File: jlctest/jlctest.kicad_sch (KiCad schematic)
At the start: 44 parts, among them Q1 MMBT5551_C2145, Q2 S8550_C105432, Q3 SI2301CDS-T1-GE3, Q4 AO3401A, Q5 D882_C9634, SW1 TS-1187A-B-A-B, U1 OP07CDR, U10 L78M05ABDT-TR, U2 TPS5430DDAR, U3 SP485EEN-L/TR, U4 W25Q128JVSIQTR, U5 LM324DT, U6 74HC595D,118, U7 SP3232EEY-L/TR, U8 AMS1117-3.3, U9 AMS1117-5.0, X1 X322516MLB4SI, X2 Q13FC1350000400, X3 X322512MSB4SI, X4 X49SM8MSD2SC, X5 X50328MSB2GI

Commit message: fixup script developed and run
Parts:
- C1: PartNumber (none) -> 0402B102K500NT
- C2: PartNumber (none) -> 0603B103K500NT
- C3: PartNumber (none) -> 0805B333K500NT
- C4: PartNumber (none) -> 1206B102K202NT
- C5: PartNumber (none) -> TAJA106K016RNJ
- C6: PartNumber (none) -> TAJB107K006RNJ
- D1: PartNumber (none) -> SS34_C8678
- D2: PartNumber (none) -> SS54_C22452
- D3: PartNumber (none) -> US1MG_C412437
- D4: PartNumber (none) -> P6SMB6.8CA-C78395
- D5: PartNumber (none) -> 1N4148W_C81598
- D6: PartNumber (none) -> SM4007PL
- D7: PartNumber (none) -> B5819W_C8598
- D8: PartNumber (none) -> 1N4148WS T4
- L1: PartNumber (none) -> GZ1608D601TF
- L2: PartNumber (none) -> GZ2012D101TF
- LED1: PartNumber (none) -> whiteLEDSMD
- Q1: PartNumber (none) -> MMBT5551_C2145
- Q2: PartNumber (none) -> S8550_C105432
- Q3: PartNumber (none) -> SI2301CDS-T1-GE3
- Q4: PartNumber (none) -> AO3401A
- Q5: PartNumber (none) -> D882_C9634
- R1: PartNumber (none) -> 0402WGF0000TCE
- R2: PartNumber (none) -> 0603WAF0000T5E
- R3: PartNumber (none) -> 0805W8F0000T5E
- R4: PartNumber (none) -> 1206W4F0000T5E
- R5: PartNumber (none) -> 0805W8F100JT5E
- RN1: PartNumber (none) -> 4D03WGJ0102T5E
- SW1: PartNumber (none) -> TS-1187A-B-A-B
- U1: PartNumber (none) -> OP07CDR
- U10: PartNumber (none) -> L78M05ABDT-TR
- U2: PartNumber (none) -> TPS5430DDAR
- U3: PartNumber (none) -> SP485EEN-L/TR
- U4: PartNumber (none) -> W25Q128JVSIQTR
- U5: PartNumber (none) -> LM324DT
- U6: PartNumber (none) -> 74HC595D,118
- U7: PartNumber (none) -> SP3232EEY-L/TR
- U8: PartNumber (none) -> AMS1117-3.3
- U9: PartNumber (none) -> AMS1117-5.0
- X1: PartNumber (none) -> X322516MLB4SI
- X2: PartNumber (none) -> Q13FC1350000400
- X3: PartNumber (none) -> X322512MSB4SI
- X4: PartNumber (none) -> X49SM8MSD2SC
- X5: PartNumber (none) -> X50328MSB2GI

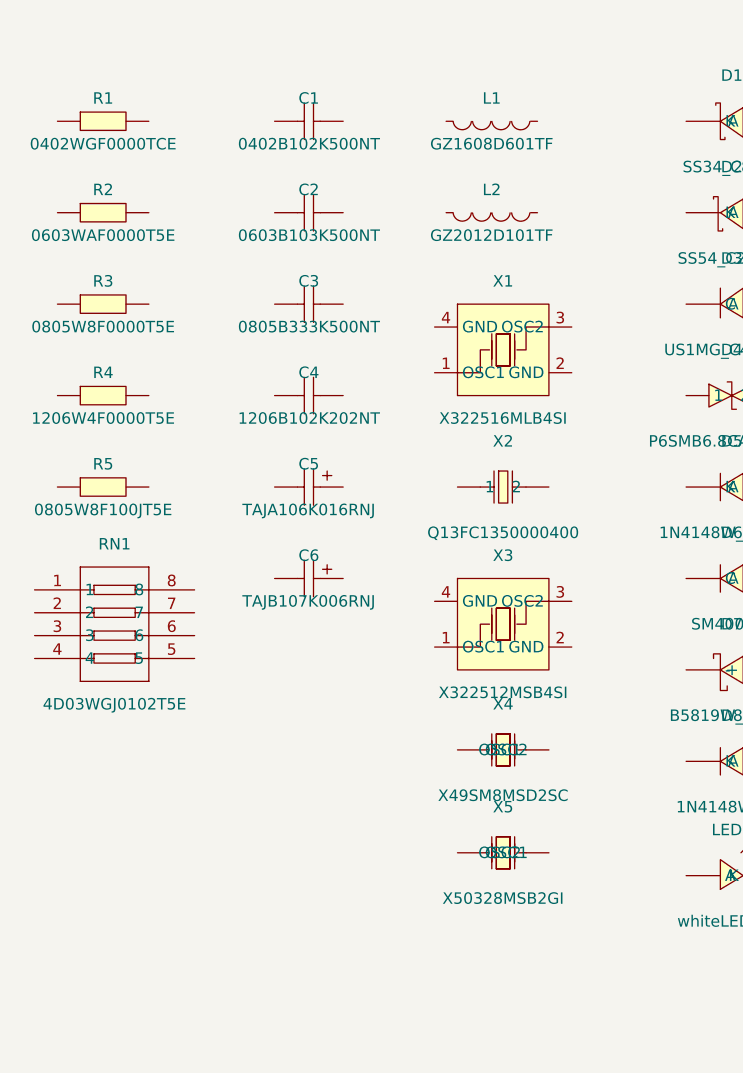
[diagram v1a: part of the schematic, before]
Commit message: Updated symbols with values and descriptions from screen scrapings
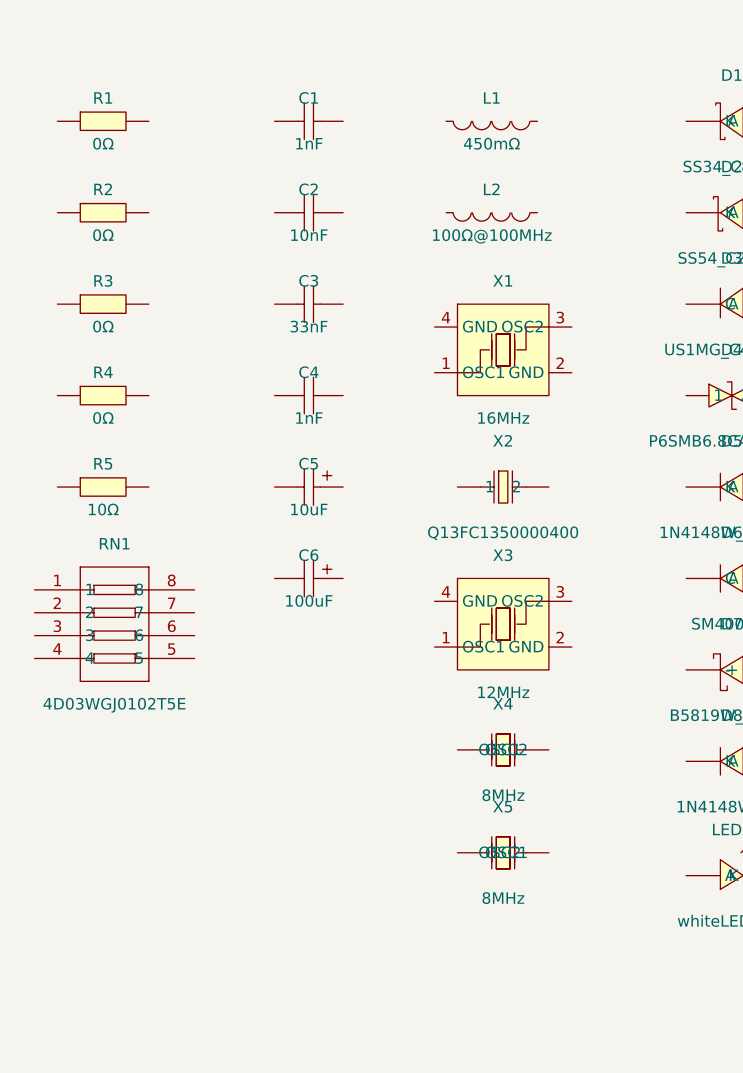
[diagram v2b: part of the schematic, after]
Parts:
- C1: value 0402B102K500NT -> 1nF
- C2: value 0603B103K500NT -> 10nF
- C3: value 0805B333K500NT -> 33nF
- C4: value 1206B102K202NT -> 1nF
- C5: value TAJA106K016RNJ -> 10uF
- C6: value TAJB107K006RNJ -> 100uF
- L1: value GZ1608D601TF -> 450mΩ
- L2: value GZ2012D101TF -> 100Ω@100MHz
- R1: value 0402WGF0000TCE -> 0Ω
- R2: value 0603WAF0000T5E -> 0Ω
- R3: value 0805W8F0000T5E -> 0Ω
- R4: value 1206W4F0000T5E -> 0Ω
- R5: value 0805W8F100JT5E -> 10Ω
- X1: value X322516MLB4SI -> 16MHz
- X3: value X322512MSB4SI -> 12MHz
- X4: value X49SM8MSD2SC -> 8MHz
- X5: value X50328MSB2GI -> 8MHz
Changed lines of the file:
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@@
 			)
 		)
-		(property "Description" ""
+		(property "Description" "235Kbps Transceiver 2/2 TSSOP-16 RS232 ICs ROHS"
 			(at 201.93 121.92 0)
 			(effects
@@
 			)
 		)
-		(property "Description" ""
+		(property "Description" "20V 3.1A 112mΩ@4.5V,2.8A 1V@250uA 1 Piece P-Channel SOT-23 MOSFETs ROHS"
 			(at 130.81 83.82 0)
 			(effects
@@
 			)
 		)
-		(property "Description" ""
+		(property "Description" "30V 4A 44mΩ@10V,4.3A 1.4W 1.3V@250uA 1 Piece P-Channel SOT-23 MOSFETs ROHS"
 			(at 129.54 97.79 0)
 			(effects
@@
 			)
 		)
-		(property "Value" "0805B333K500NT"
+		(property "Value" "33nF"
 			(at 66.04 76.2 0)
 			(effects
@@
 			)
 		)
-		(property "Description" ""
+		(property "Description" "50V 33nF X7R ±10% 0805 Multilayer Ceramic Capacitors MLCC - SMD/SMT ROHS"
 			(at 66.04 73.66 0)
 			(effects
@@
 			)
 		)
-		(property "Value" "TAJA106K016RNJ"
+		(property "Value" "10uF"
 			(at 66.04 96.52 0)
 			(effects
@@
 			)
 		)
-		(property "Description" ""
+		(property "Description" "10uF 16V 3Ω@100kHz ±10% CASE-A-3216-18(mm) Tantalum Capacitors ROHS"
 			(at 66.04 93.98 0)
 			(effects
@@
 			)
 		)
-		(property "Value" "1206B102K202NT"
+		(property "Value" "1nF"
 			(at 66.04 86.36 0)
 			(effects
@@
 			)
 		)
-		(property "Description" ""
+		(property "Description" "2kV 1nF X7R ±10% 1206 Multilayer Ceramic Capacitors MLCC - SMD/SMT ROHS"
 			(at 66.04 83.82 0)
 			(effects
@@
 			)
 		)
-		(property "Description" ""
+		(property "Description" "8 2V~6V 1 Serial to serial or parallel SOIC-16 Shift Registers ROHS"
 			(at 201.93 91.44 0)
 			(effects
@@
 			)
 		)
-		(property "Value" "0402WGF0000TCE"
+		(property "Value" "0Ω"
 			(at 43.18 55.88 0)
 			(effects
@@
 			)
 		)
-		(property "Description" ""
+		(property "Description" "62.5mW Thick Film Resistors 50V ±800ppm/℃ ±1% 0Ω 0402 Chip Resistor - Surface Mount ROHS"
 			(at 43.18 53.34 0)
 			(effects
@@
 			)
 		)
-		(property "Description" ""
+		(property "Description" "1A Independent Type 1kV 1.1V@1A SOD-123FL Diodes - General Purpose ROHS"
 			(at 113.03 104.14 0)
 			(effects
@@
 			)
 		)
-		(property "Description" ""
+		(property "Description" "Quad 20nA 0.4V/us 1.3MHz SOIC-14 Operational Amplifier ROHS"
 			(at 201.93 60.96 0)
 			(effects
@@
 			)
 		)
-		(property "Value" "TAJB107K006RNJ"
+		(property "Value" "100uF"
 			(at 66.04 106.68 0)
 			(effects
@@
 			)
 		)
-		(property "Description" ""
+		(property "Description" "100uF 6.3V 1.7Ω@100kHz ±10% CASE-B-3528-21(mm) Tantalum Capacitors ROHS"
 			(at 66.04 104.14 0)
 			(effects
@@
 			)
 		)
-		(property "Description" ""
+		(property "Description" "Transceiver 10Mbps 1/1 SOIC-8 RS-485 / RS-422 ICs ROHS"
 			(at 166.37 115.57 0)
 			(effects
@@
 			)
 		)
-		(property "Value" "GZ1608D601TF"
+		(property "Value" "450mΩ"
 			(at 86.36 55.88 0)
 			(effects
@@
 			)
 		)
-		(property "Description" ""
+		(property "Description" "450mΩ ±25% 600Ω@100MHz 0603 Ferrite Beads ROHS"
 			(at 86.36 53.34 0)
 			(effects
@@
 			)
 		)
-		(property "Description" ""
+		(property "Description" "None Without 50mA 5.1mm 100000 Times 160gf 12V 5.1mm 1.5mm Round Button Standing paste SPST SMD Tactile Switches ROHS"
 			(at 234.95 120.65 0)
 			(effects
@@
 			)
 		)
-		(property "Description" ""
+		(property "Description" "600kHz 1.8nA Single Channel SOIC-8 Precision Op Amps ROHS"
 			(at 163.83 60.96 0)
 			(effects
@@
 			)
 		)
-		(property "Value" "X49SM8MSD2SC"
+		(property "Value" "8MHz"
 			(at 87.63 128.27 0)
 			(effects
@@
 			)
 		)
-		(property "Description" ""
+		(property "Description" "8MHz Surface Mount Crystal 20pF ±20ppm ±30ppm HC-49S-SMD Crystals ROHS"
 			(at 87.63 123.19 0)
 			(effects
@@
 			)
 		)
-		(property "Description" ""
+		(property "Description" "Step-down type Adjustable 1.221V~32.04V 3A 5.5V~36V SOIC-8-EP DC-DC Converters ROHS"
 			(at 165.1 90.17 0)
 			(effects
@@
 			)
 		)
-		(property "Value" "X50328MSB2GI"
+		(property "Value" "8MHz"
 			(at 87.63 139.7 0)
 			(effects
@@
 			)
 		)
-		(property "Description" ""
+		(property "Description" "8MHz Surface Mount Crystal 20pF ±10ppm ±20ppm SMD5032 Crystals ROHS"
 			(at 87.63 134.62 0)
 			(effects
@@
 			)
 		)
-		(property "Value" "1206W4F0000T5E"
+		(property "Value" "0Ω"
 			(at 43.18 86.36 0)
 			(effects
@@
 			)
 		)
-		(property "Description" ""
+		(property "Description" "250mW Thick Film Resistors 200V ±800ppm/℃ ±1% 0Ω 1206 Chip Resistor - Surface Mount ROHS"
 			(at 43.18 83.82 0)
 			(effects
@@
 			)
 		)
-		(property "Value" "0603WAF0000T5E"
+		(property "Value" "0Ω"
 			(at 43.18 66.04 0)
 			(effects
@@
 			)
 		)
-		(property "Description" ""
+		(property "Description" "100mW Thick Film Resistors 75V ±1% 0Ω 0603 Chip Resistor - Surface Mount ROHS"
 			(at 43.18 63.5 0)
 			(effects
@@
 			)
 		)
-		(property "Description" ""
+		(property "Description" "4 ±5% 1kΩ 62.5mW ±200ppm/℃ 0603x4 Resistor Networks, Arrays ROHS"
 			(at 44.45 109.22 0)
 			(effects
@@
 			)
 		)
-		(property "Value" "0603B103K500NT"
+		(property "Value" "10nF"
 			(at 66.04 66.04 0)
 			(effects
@@
 			)
 		)
-		(property "Description" ""
+		(property "Description" "50V 10nF X7R ±10% 0603 Multilayer Ceramic Capacitors MLCC - SMD/SMT ROHS"
 			(at 66.04 63.5 0)
 			(effects
@@
 			)
 		)
-		(property "Description" ""
+		(property "Description" "72dB@(120Hz) 1A Fixed 3.3V Positive electrode SOT-223 Voltage Regulators - Linear, Low Drop Out (LDO) Regulators ROHS"
 			(at 234.95 55.88 0)
 			(effects
@@
 			)
 		)
-		(property "Value" "GZ2012D101TF"
+		(property "Value" "100Ω@100MHz"
 			(at 86.36 66.04 0)
 			(effects
@@
 			)
 		)
-		(property "Description" ""
+		(property "Description" "±25% 100Ω@100MHz 0805 Ferrite Beads ROHS"
 			(at 86.36 63.5 0)
 			(effects
@@
 			)
 		)
-		(property "Value" "X322512MSB4SI"
+		(property "Value" "12MHz"
 			(at 87.63 116.84 0)
 			(effects
@@
 			)
 		)
-		(property "Description" ""
+		(property "Description" "12MHz Surface Mount Crystal 20pF ±10ppm ±20ppm SMD3225-4P Crystals ROHS"
 			(at 87.63 109.22 0)
 			(effects
@@
 			)
 		)
-		(property "Value" "0402B102K500NT"
+		(property "Value" "1nF"
 			(at 66.04 55.88 0)
 			(effects
@@
 			)
 		)
-		(property "Description" ""
+		(property "Description" "50V 1nF X7R ±10% 0402 Multilayer Ceramic Capacitors MLCC - SMD/SMT ROHS"
 			(at 66.04 53.34 0)
 			(effects
@@
 			)
 		)
-		(property "Value" "0805W8F100JT5E"
+		(property "Value" "10Ω"
 			(at 43.18 96.52 0)
 			(effects
@@
 			)
 		)
-		(property "Description" ""
+		(property "Description" "125mW Thick Film Resistors 150V ±1% ±200ppm/℃ 10Ω 0805 Chip Resistor - Surface Mount ROHS"
 			(at 43.18 93.98 0)
 			(effects
@@
 			)
 		)
-		(property "Value" "0805W8F0000T5E"
+		(property "Value" "0Ω"
 			(at 43.18 76.2 0)
 			(effects
@@
 			)
 		)
-		(property "Description" ""
+		(property "Description" "125mW Thick Film Resistors 150V ±800ppm/℃ ±1% 0Ω 0805 Chip Resistor - Surface Mount ROHS"
 			(at 43.18 73.66 0)
 			(effects
@@
 			)
 		)
-		(property "Description" ""
+		(property "Description" "68dB@(120Hz) 1A Fixed 5V Positive electrode 12V SOT-223 Voltage Regulators - Linear, Low Drop Out (LDO) Regulators ROHS"
 			(at 234.95 74.93 0)
 			(effects
@@
 			)
 		)
-		(property "Description" ""
+		(property "Description" "62dB@(120Hz) 500mA Fixed 5V Positive electrode 35V TO-252-2(DPAK) Voltage Regulators - Linear, Low Drop Out (LDO) Regulators ROHS"
 			(at 234.95 99.06 0)
 			(effects
@@
 			)
 		)
-		(property "Value" "X322516MLB4SI"
+		(property "Value" "16MHz"
 			(at 87.63 86.36 0)
 			(effects
@@
 			)
 		)
-		(property "Description" ""
+		(property "Description" "16MHz Surface Mount Crystal 9pF ±10ppm ±20ppm SMD3225-4P Crystals ROHS"
 			(at 87.63 78.74 0)
 			(effects

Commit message: Aesthetic manual cleanup of all components not handled by the batch update
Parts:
- D1: value SS34_C8678 -> SS34
- D2: value SS54_C22452 -> SS54
- D3: value US1MG_C412437 -> US1MG
- D4: value P6SMB6.8CA-C78395 -> P6SMB6.8CA
- D5: value 1N4148W_C81598 -> 1N4148W
- D7: value B5819W_C8598 -> B5819W
- D8: value 1N4148WS T4 -> 1N4148ST4
- L1: value 450mΩ -> 600Ω@100MHz
- Q1: value MMBT5551_C2145 -> MMBT5551
- Q2: value S8550_C105432 -> S8550; PartNumber S8550_C105432 -> S8550
- Q3: value SI2301CDS-T1-GE3 -> SI2301CDS
- Q5: value D882_C9634 -> D882
- RN1: value 4D03WGJ0102T5E -> 1KΩ
- U10: value L78M05ABDT-TR -> L78M05
- U3: value SP485EEN-L/TR -> SP485EEN
- U6: value 74HC595D,118 -> 74HC595
- U7: value SP3232EEY-L/TR -> SP3232EEY
- X2: value Q13FC1350000400 -> 32.768kHz

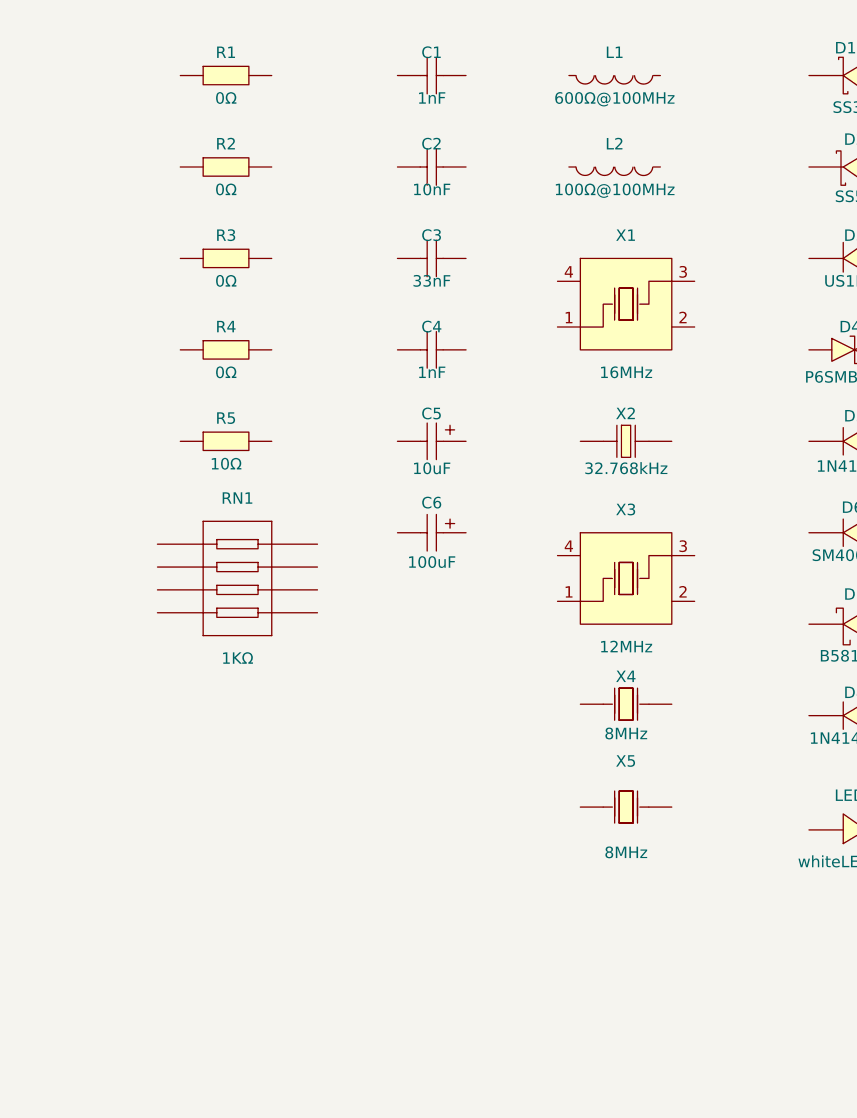
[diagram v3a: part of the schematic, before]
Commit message: Adopted some more compact syntax
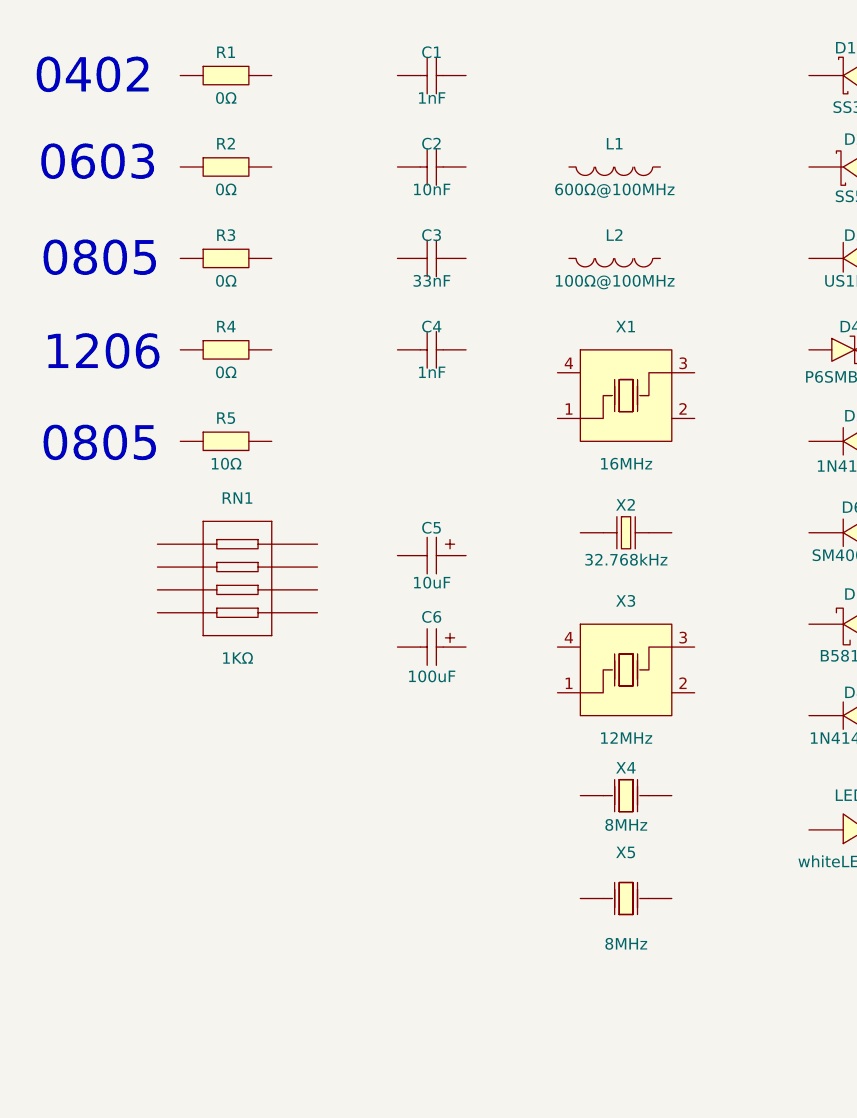
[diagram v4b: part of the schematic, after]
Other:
- note added: "0402"
- note added: "0603"
- note added: "0805"
- note added: "1206"
- moved on the sheet: C5, C6, L1, L2, X1, X2, X3, X4, X5

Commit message: Renamed all symbols to have more semantic names where possible
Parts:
- C1: symbol jlcbasic:0402B102K500NT -> jlcbasic:1nF-0402; PartNumber 0402B102K500NT -> 1nF-0402
- C2: symbol jlcbasic:0603B103K500NT -> jlcbasic:10nF-0603; PartNumber 0603B103K500NT -> 10nF-0603
- C3: symbol jlcbasic:0805B333K500NT -> jlcbasic:33nF-0805; PartNumber 0805B333K500NT -> 33nF-0805
- C4: symbol jlcbasic:1206B102K202NT -> jlcbasic:1nF-1206; PartNumber 1206B102K202NT -> 1nF-1206
- L1: symbol jlcbasic:GZ1608D601TF -> jlcbasic:600Ω@100MHz-0603; PartNumber GZ1608D601TF -> 600Ω@100MHz-0603
- L2: symbol jlcbasic:GZ2012D101TF -> jlcbasic:100Ω@100MHz-0805; PartNumber GZ2012D101TF -> 100Ω@100MHz-0805
- R1: symbol jlcbasic:0402WGF0000TCE -> jlcbasic:0Ω-0402; PartNumber 0402WGF0000TCE -> 0Ω-0402
- R2: symbol jlcbasic:0603WAF0000T5E -> jlcbasic:0Ω-0603; PartNumber 0603WAF0000T5E -> 0Ω-0603
- R3: symbol jlcbasic:0805W8F0000T5E -> jlcbasic:0Ω-0805; PartNumber 0805W8F0000T5E -> 0Ω-0805
- R4: symbol jlcbasic:1206W4F0000T5E -> jlcbasic:0Ω-1206; PartNumber 1206W4F0000T5E -> 0Ω-1206
- R5: symbol jlcbasic:0805W8F100JT5E -> jlcbasic:10Ω-0805; PartNumber 0805W8F100JT5E -> 10Ω-0805
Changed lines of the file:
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@@
 	)
 	(symbol
-		(lib_id "jlcbasic:0805B333K500NT")
+		(lib_id "jlcbasic:33nF-0805")
 		(at 66.04 73.66 0)
 		(unit 1)
@@
 			)
 		)
-		(property "PartNumber" "0805B333K500NT"
+		(property "PartNumber" "33nF-0805"
 			(at 66.04 73.66 0)
 			(effects
@@
 	)
 	(symbol
-		(lib_id "jlcbasic:1206B102K202NT")
+		(lib_id "jlcbasic:1nF-1206")
 		(at 66.04 83.82 0)
 		(unit 1)
@@
 			)
 		)
-		(property "PartNumber" "1206B102K202NT"
+		(property "PartNumber" "1nF-1206"
 			(at 66.04 83.82 0)
 			(effects
@@
 	)
 	(symbol
-		(lib_id "jlcbasic:0402WGF0000TCE")
+		(lib_id "jlcbasic:0Ω-0402")
 		(at 43.18 53.34 0)
 		(unit 1)
@@
 			)
 		)
-		(property "PartNumber" "0402WGF0000TCE"
+		(property "PartNumber" "0Ω-0402"
 			(at 43.18 53.34 0)
 			(effects
@@
 	)
 	(symbol
-		(lib_id "jlcbasic:GZ1608D601TF")
+		(lib_id "jlcbasic:600Ω@100MHz-0603")
 		(at 86.36 63.5 0)
 		(unit 1)
@@
 			)
 		)
-		(property "PartNumber" "GZ1608D601TF"
+		(property "PartNumber" "600Ω@100MHz-0603"
 			(at 86.36 63.5 0)
 			(effects
@@
 	)
 	(symbol
-		(lib_id "jlcbasic:1206W4F0000T5E")
+		(lib_id "jlcbasic:0Ω-1206")
 		(at 43.18 83.82 0)
 		(unit 1)
@@
 			)
 		)
-		(property "PartNumber" "1206W4F0000T5E"
+		(property "PartNumber" "0Ω-1206"
 			(at 43.18 83.82 0)
 			(effects
@@
 	)
 	(symbol
-		(lib_id "jlcbasic:0603WAF0000T5E")
+		(lib_id "jlcbasic:0Ω-0603")
 		(at 43.18 63.5 0)
 		(unit 1)
@@
 			)
 		)
-		(property "PartNumber" "0603WAF0000T5E"
+		(property "PartNumber" "0Ω-0603"
 			(at 43.18 63.5 0)
 			(effects
@@
 	)
 	(symbol
-		(lib_id "jlcbasic:0603B103K500NT")
+		(lib_id "jlcbasic:10nF-0603")
 		(at 66.04 63.5 0)
 		(unit 1)
@@
 			)
 		)
-		(property "PartNumber" "0603B103K500NT"
+		(property "PartNumber" "10nF-0603"
 			(at 66.04 63.5 0)
 			(effects
@@
 	)
 	(symbol
-		(lib_id "jlcbasic:GZ2012D101TF")
+		(lib_id "jlcbasic:100Ω@100MHz-0805")
 		(at 86.36 73.66 0)
 		(unit 1)
@@
 			)
 		)
-		(property "PartNumber" "GZ2012D101TF"
+		(property "PartNumber" "100Ω@100MHz-0805"
 			(at 86.36 73.66 0)
 			(effects
@@
 	)
 	(symbol
-		(lib_id "jlcbasic:0402B102K500NT")
+		(lib_id "jlcbasic:1nF-0402")
 		(at 66.04 53.34 0)
 		(unit 1)
@@
 			)
 		)
-		(property "PartNumber" "0402B102K500NT"
+		(property "PartNumber" "1nF-0402"
 			(at 66.04 53.34 0)
 			(effects
@@
 	)
 	(symbol
-		(lib_id "jlcbasic:0805W8F100JT5E")
+		(lib_id "jlcbasic:10Ω-0805")
 		(at 43.18 93.98 0)
 		(unit 1)
@@
 			)
 		)
-		(property "PartNumber" "0805W8F100JT5E"
+		(property "PartNumber" "10Ω-0805"
 			(at 43.18 93.98 0)
 			(effects
@@
 	)
 	(symbol
-		(lib_id "jlcbasic:0805W8F0000T5E")
+		(lib_id "jlcbasic:0Ω-0805")
 		(at 43.18 73.66 0)
 		(unit 1)
@@
 			)
 		)
-		(property "PartNumber" "0805W8F0000T5E"
+		(property "PartNumber" "0Ω-0805"
 			(at 43.18 73.66 0)
 			(effects
